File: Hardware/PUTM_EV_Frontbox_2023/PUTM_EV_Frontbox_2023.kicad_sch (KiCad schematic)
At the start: 18 parts, among them J1 Conn_02x16_Counter_Clockwise, J2 Conn_01x04, SW1 Reset switch, U1 STM32G473RCTx

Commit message: Started PCB layout
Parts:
- removed R102: 10k, Resistor_SMD:R_0603_1608Metric_Pad0.98x0.95mm_HandSolder, symbol Device:R_Small
- added H1, H2, H3, H4: MountingHole_Pad, MountingHole:MountingHole_3.2mm_M3_DIN965_Pad_TopBottom, symbol Mechanical:MountingHole_Pad
- J1: footprint (none) -> Connector_PinHeader_2.54mm:PinHeader_2x16_P2.54mm_Vertical
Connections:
- net +24V: now also J1.31 (Pin_31); no longer J1.32 (Pin_32)
- net +5V: now also J1.32 (Pin_32); no longer J1.31 (Pin_31)
- net APPS_POT_1: now also J1.2 (Pin_2); no longer J1.21 (Pin_21)
- net APPS_POT_2: now also J1.1 (Pin_1); no longer J1.20 (Pin_20)
- net BRAKE_POSITION_IN: now also J1.4 (Pin_4); no longer J1.24 (Pin_24)
- net BRAKE_PRESSURE1_IN: now also J1.9 (Pin_9); no longer J1.13 (Pin_13)
- net BSPD_SENSE: now also J1.19 (Pin_19); no longer J1.1 (Pin_1)
- net CAN1+: now also J1.29 (Pin_29); no longer J1.28 (Pin_28)
- net CAN1-: now also J1.28 (Pin_28); no longer J1.29 (Pin_29)
- net CAN2+: now also J1.27 (Pin_27); no longer J1.26 (Pin_26)
- net CAN2-: now also J1.26 (Pin_26); no longer J1.27 (Pin_27)
- net EBS_SAFETY: now also J1.25 (Pin_25); no longer J1.7 (Pin_7)
- net GND: now also R57.1, R58.1, H1.1, H2.1, H3.1, H4.1; no longer R57.2, R58.2
- net INERTIA: now also J1.24 (Pin_24); no longer J1.6 (Pin_6)
- net KILL_KIERA: now also J1.23 (Pin_23); no longer J1.5 (Pin_5)
- net KILL_LEWY: now also J1.22 (Pin_22); no longer J1.4 (Pin_4)
- net KILL_PRAWY: now also J1.20 (Pin_20); no longer J1.2 (Pin_2)
- net OVERTRAVEL: now also J1.21 (Pin_21); no longer J1.3 (Pin_3)
- net SAFE-IN: now also J1.13 (Pin_13); no longer J1.8 (Pin_8)
- net SAFE-OUT: now also J1.14 (Pin_14); no longer J1.9 (Pin_9)
- net STEERING_POSITION_IN: now also J1.5 (Pin_5); no longer J1.25 (Pin_25)
- net SUSPENSION_POT1_IN: now also J1.11 (Pin_11); no longer J1.19 (Pin_19)
- net SUSPENSION_POT2_IN: now also J1.10 (Pin_10); no longer J1.14 (Pin_14)
- net at R48.2: now also J1.18 (Pin_18); no longer J1.11 (Pin_11)
- net at R6.2: now also J1.17 (Pin_17); no longer J1.10 (Pin_10)
- net at J1.15 (Pin_15): now also R58.2
- net at J1.16 (Pin_16): now also R57.2
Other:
- removed sheet Brake Position Potentiometer
- removed sheet Steering Wheel Angle
- added sheet Brake Position (suspension_potentiometer.kicad_sch)
- added sheet CAN bus1 (can_bus.kicad_sch)
- added sheet Steering Position (suspension_potentiometer.kicad_sch)
- sheet APPS1 ports: added 3V3_POT1; removed none
- sheet APPS2: file APPS1.kicad_sch -> APPS2.kicad_sch
- sheet APPS2 ports: added 3V3_POT2, OUT1; removed OUT2
- note added: "APPS Measurement"
- note added: "Analog Inputs"
- note added: "CAN Bus"
- note added: "Debug LEDs"
- note added: "Digital Inputs"
- note added: "MCU"
- note added: "MCU Circutry"
- note added: "Main Connector"
- note added: "Mounting Holes"
- note added: "Power Supply"
- note added: "SC Control"
- note added: "SC sensing"
- note removed: "Horizontal goldpin connector"
- company: Author: Szymon Kostrubiec -> Author: Adam Wasilewski
- moved on the sheet: C1, D1, D2, D3, D4, J2, R1, R2, R3, R4, R48, R57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

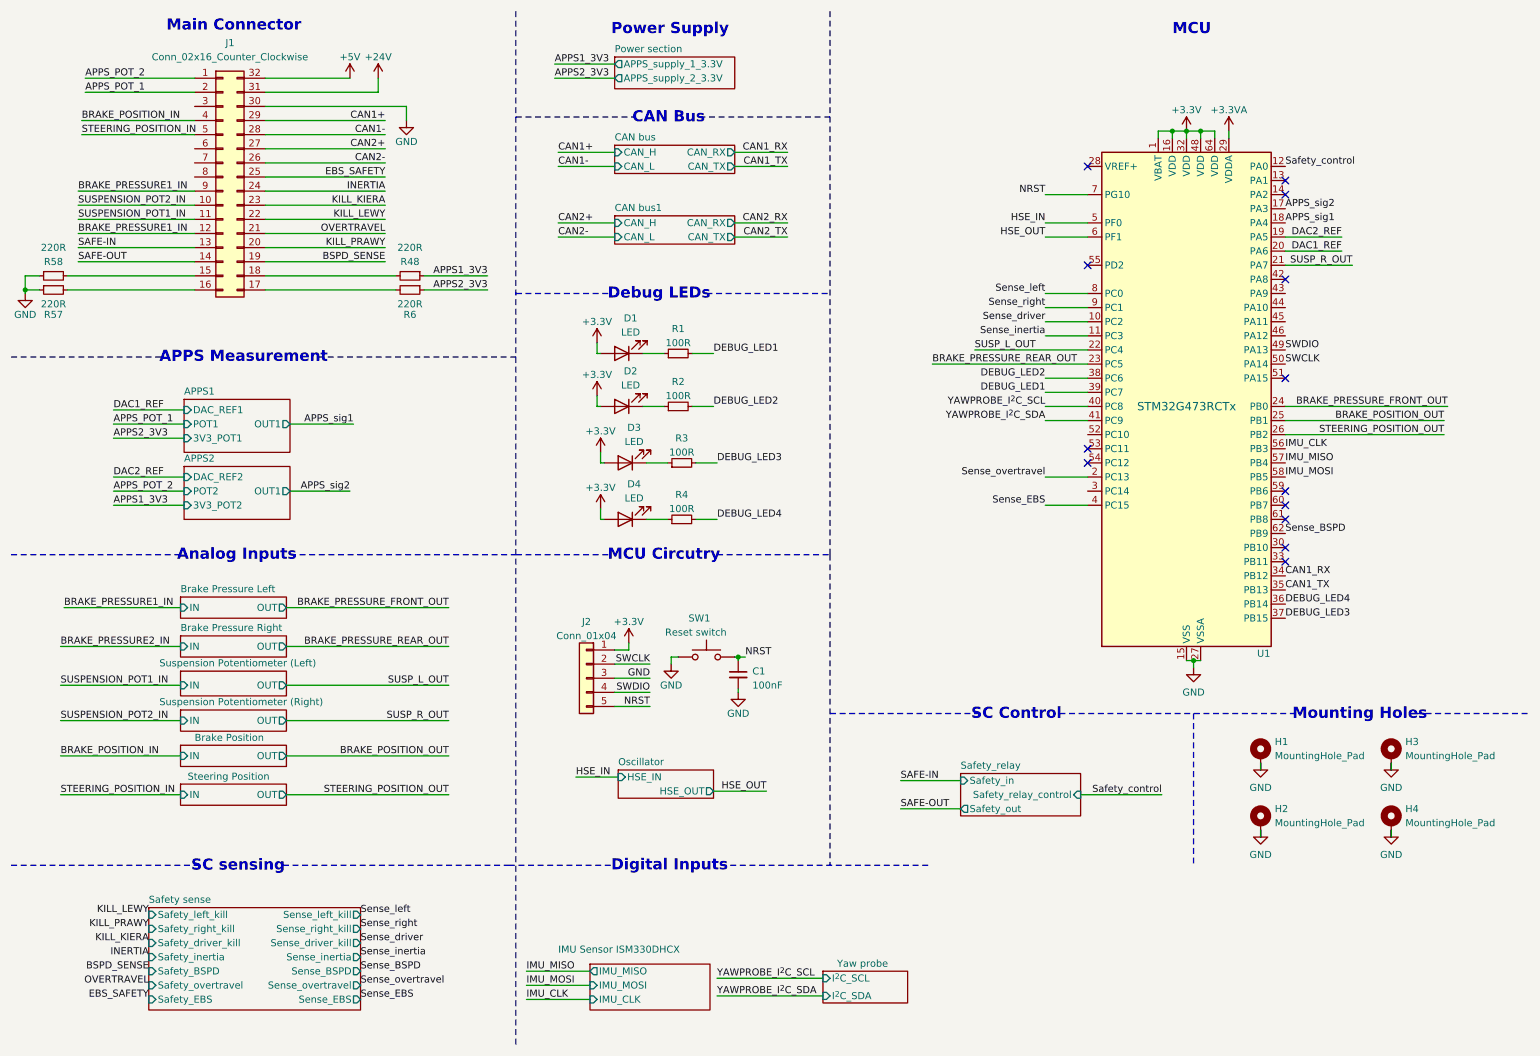
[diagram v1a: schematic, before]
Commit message: Changed board outline and layout to match ASB
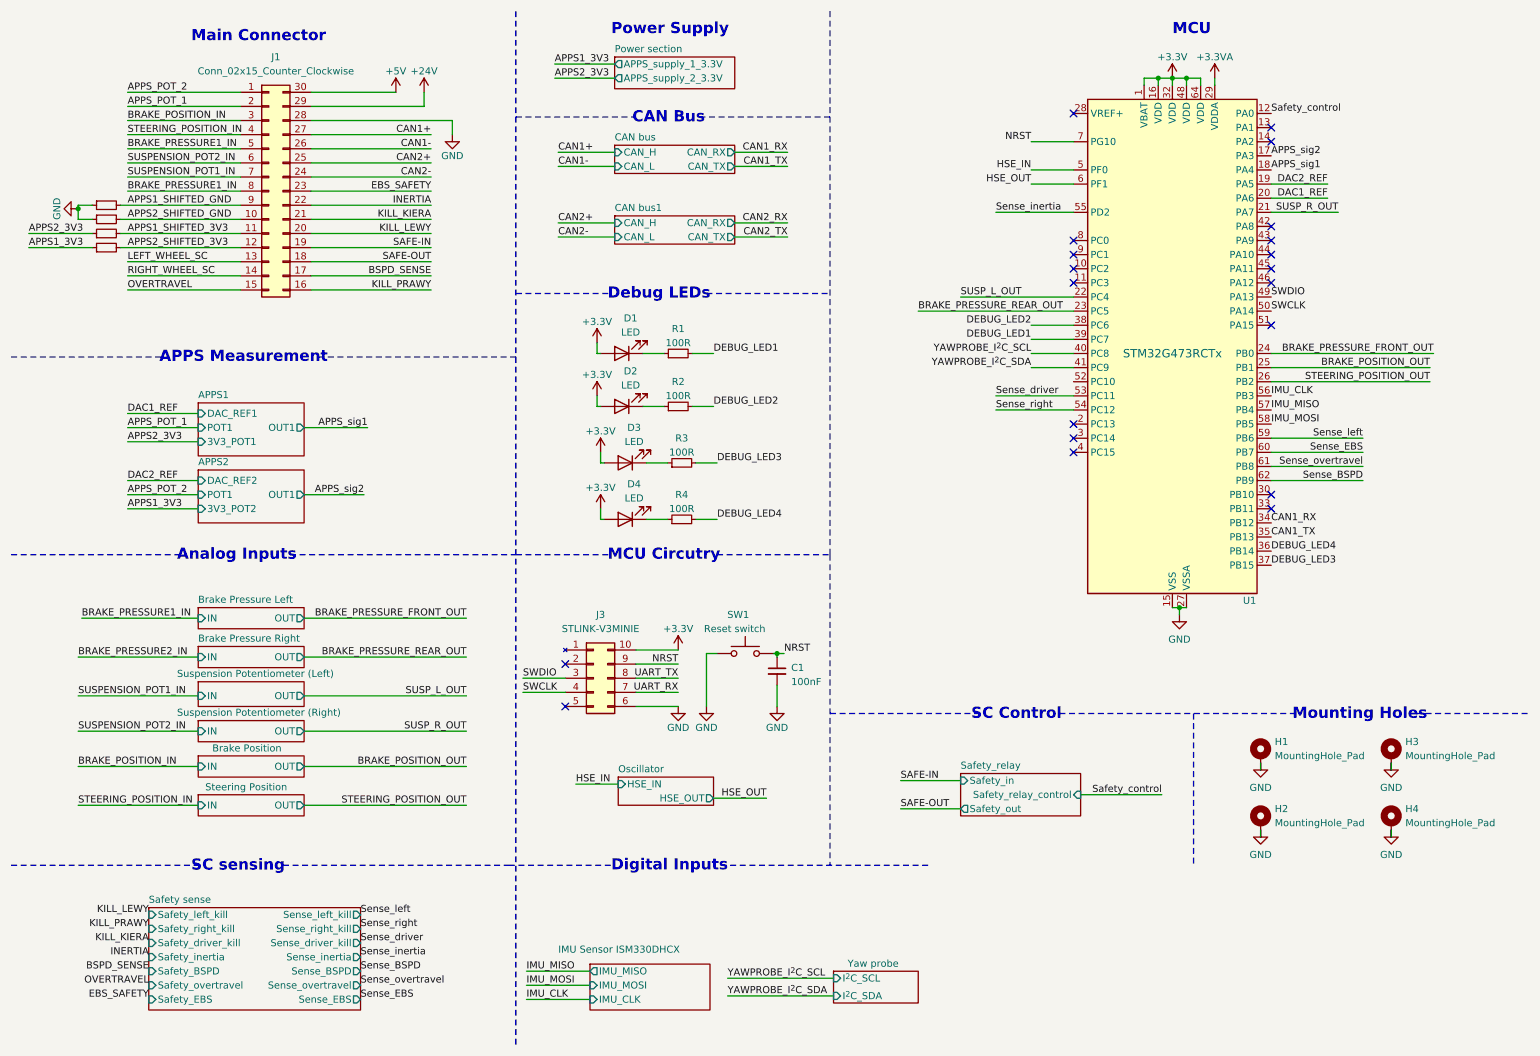
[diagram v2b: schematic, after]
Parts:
- removed J1: Conn_02x16_Counter_Clockwise, Connector_PinHeader_2.54mm:PinHeader_2x16_P2.54mm_Vertical, symbol Connector_Generic:Conn_02x16_Counter_Clockwise
- removed J2: Conn_01x04, Connector_PinHeader_2.54mm:PinHeader_1x05_P2.54mm_Vertical, symbol Connector_Generic:Conn_01x05
- added J1: Conn_02x15_Counter_Clockwise, Connector_IDC:IDC-Header_2x15-1MP_P2.54mm_Latch6.5mm_Vertical, symbol Connector_Generic:Conn_02x15_Counter_Clockwise
- added J3: STLINK-V3MINIE, Frontbox:STLINK-V3MINIE, symbol FrontBox:STLINK-V3MINIE
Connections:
- net +24V: now also J1.29 (Pin_29)
- net +3.3V: now also J3.10 (T_VCC)
- net +5V: now also J1.30 (Pin_30)
- net APPS_POT_1: now also J1.2 (Pin_2)
- net APPS_POT_2: now also J1.1 (Pin_1)
- net BRAKE_POSITION_IN: now also J1.3 (Pin_3)
- net BRAKE_PRESSURE1_IN: now also J1.5 (Pin_5), J1.8 (Pin_8)
- net BSPD_SENSE: now also J1.17 (Pin_17)
- net CAN1+: now also J1.27 (Pin_27)
- net CAN1-: now also J1.26 (Pin_26)
- net CAN2+: now also J1.25 (Pin_25)
- net CAN2-: now also J1.24 (Pin_24)
- net EBS_SAFETY: now also J1.23 (Pin_23)
- net GND: now also J1.28 (Pin_28), J3.6 (GND)
- net INERTIA: now also J1.22 (Pin_22)
- net KILL_KIERA: now also J1.21 (Pin_21)
- net KILL_LEWY: now also J1.20 (Pin_20)
- net KILL_PRAWY: now also J1.16 (Pin_16)
- net NRST: now also J3.9 (T_NRST)
- net OVERTRAVEL: now also J1.15 (Pin_15)
- net SAFE-IN: now also J1.19 (Pin_19)
- net SAFE-OUT: now also J1.18 (Pin_18)
- net STEERING_POSITION_IN: now also J1.4 (Pin_4)
- net SUSPENSION_POT1_IN: now also J1.7 (Pin_7)
- net SUSPENSION_POT2_IN: now also J1.6 (Pin_6)
- net SWCLK: now also J3.4 (T_JCLK/T_SWCLK)
- net SWDIO: now also J3.3 (T_JTMS/T_SWDIO)
- net Sense_EBS: now also U1.60 (PB7); no longer U1.4 (PC15)
- net Sense_driver: now also U1.53 (PC11); no longer U1.10 (PC2)
- net Sense_inertia: now also U1.55 (PD2); no longer U1.11 (PC3)
- net Sense_left: now also U1.59 (PB6); no longer U1.8 (PC0)
- net Sense_overtravel: now also U1.61 (PB8); no longer U1.2 (PC13)
- net Sense_right: now also U1.54 (PC12); no longer U1.9 (PC1)
- net APPS2_SHIFTED_3V3: now reaches R48.2
- net APPS2_SHIFTED_3V3: now also J1.12 (Pin_12)
- net APPS1_SHIFTED_GND: now reaches R58.2
- net APPS1_SHIFTED_GND: now also J1.9 (Pin_9)
- net APPS2_SHIFTED_GND: now reaches R57.2
- net APPS2_SHIFTED_GND: now also J1.10 (Pin_10)
- net APPS1_SHIFTED_3V3: now reaches R6.2
- net APPS1_SHIFTED_3V3: now also J1.11 (Pin_11)
- new net LEFT_WHEEL_SC: J1.13 (Pin_13)
- new net RIGHT_WHEEL_SC: J1.14 (Pin_14)
- new net UART_RX: J3.7 (T_VCP_RX)
- new net UART_TX: J3.8 (T_VCP_TX)
- no-connect marks 13 -> 20
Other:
- sheet APPS2 ports: added POT1; removed POT2
- moved on the sheet: C1, SW1, U1

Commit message: Routing
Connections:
- net CAN1+: now also J1.25 (Pin_25); no longer J1.27 (Pin_27)
- net CAN1-: now also J1.24 (Pin_24); no longer J1.26 (Pin_26)
- net CAN2+: now also J1.27 (Pin_27); no longer J1.25 (Pin_25)
- net CAN2-: now also J1.26 (Pin_26); no longer J1.24 (Pin_24)
- net EBS_SAFETY: now also J1.19 (Pin_19); no longer J1.23 (Pin_23)
- net INERTIA: now also J1.18 (Pin_18); no longer J1.22 (Pin_22)
- net SAFE-IN: now also J1.23 (Pin_23); no longer J1.19 (Pin_19)
- net SAFE-OUT: now also J1.22 (Pin_22); no longer J1.18 (Pin_18)
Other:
- sheet APPS1 ports: added 3V3_POT, DAC_REF, OUT, POT; removed 3V3_POT1, DAC_REF1, OUT1, POT1
- sheet APPS2: file APPS2.kicad_sch -> APPS1.kicad_sch
- sheet APPS2 ports: added 3V3_POT, DAC_REF, OUT, POT; removed 3V3_POT2, DAC_REF2, OUT1, POT1

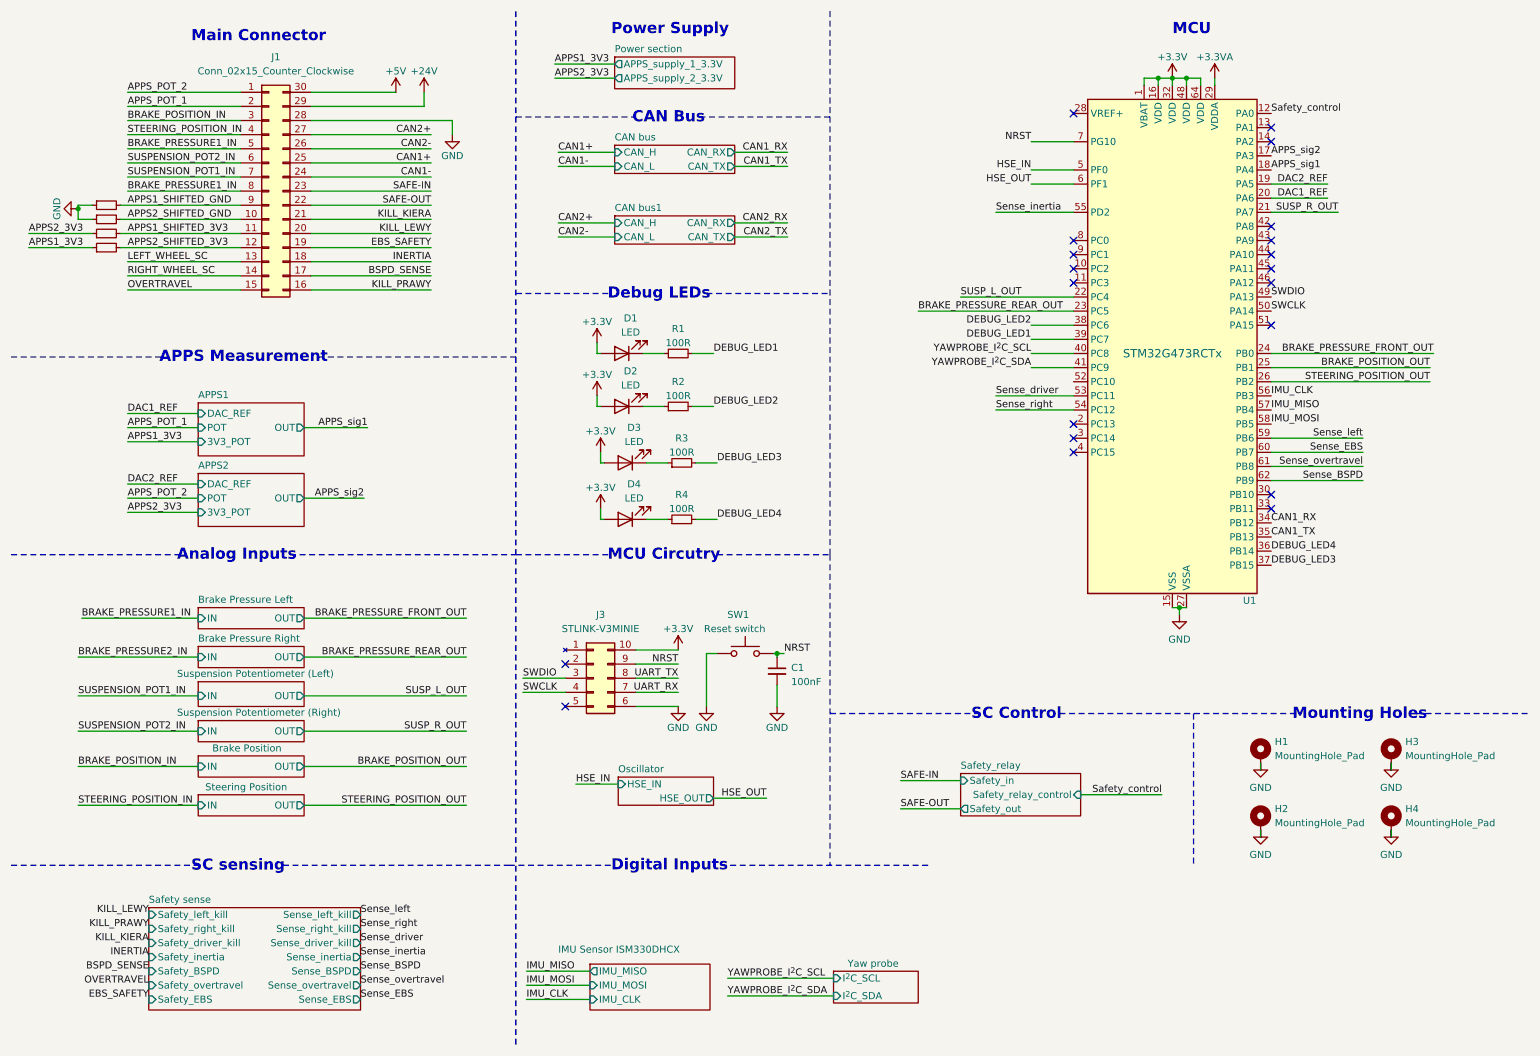
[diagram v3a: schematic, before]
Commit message: Changed mcu pinout
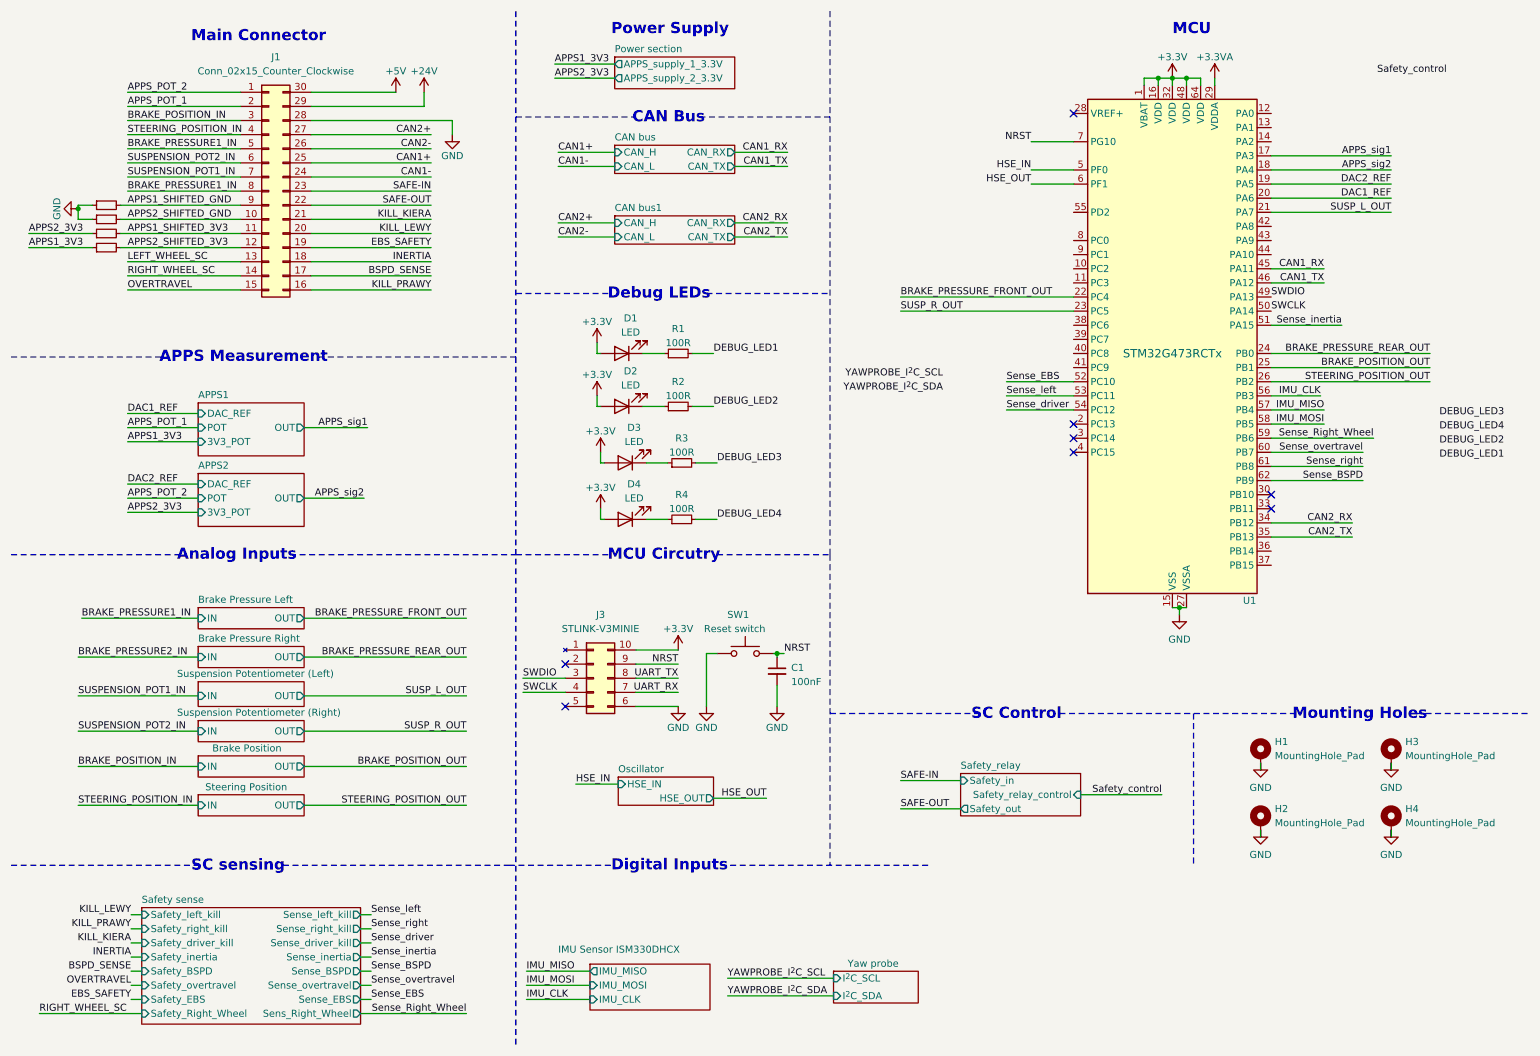
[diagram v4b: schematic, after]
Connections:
- net APPS_sig1: now also U1.17 (PA3); no longer U1.18 (PA4)
- net APPS_sig2: now also U1.18 (PA4); no longer U1.17 (PA3)
- net BRAKE_PRESSURE_FRONT_OUT: now also U1.22 (PC4); no longer U1.24 (PB0)
- net BRAKE_PRESSURE_REAR_OUT: now also U1.24 (PB0); no longer U1.23 (PC5)
- net CAN1_RX: now also U1.45 (PA11); no longer U1.34 (PB12)
- net CAN1_TX: now also U1.46 (PA12); no longer U1.35 (PB13)
- net CAN2_RX: now also U1.34 (PB12)
- net CAN2_TX: now also U1.35 (PB13)
- net DEBUG_LED1: no longer U1.39 (PC7)
- net DEBUG_LED2: no longer U1.38 (PC6)
- net DEBUG_LED3: no longer U1.37 (PB15)
- net DEBUG_LED4: no longer U1.36 (PB14)
- net SUSP_L_OUT: now also U1.21 (PA7); no longer U1.22 (PC4)
- net SUSP_R_OUT: now also U1.23 (PC5); no longer U1.21 (PA7)
- net Safety_control: no longer U1.12 (PA0)
- net Sense_EBS: now also U1.52 (PC10); no longer U1.60 (PB7)
- net Sense_driver: now also U1.54 (PC12); no longer U1.53 (PC11)
- net Sense_inertia: now also U1.51 (PA15); no longer U1.55 (PD2)
- net Sense_left: now also U1.53 (PC11); no longer U1.59 (PB6)
- net Sense_overtravel: now also U1.60 (PB7); no longer U1.61 (PB8)
- net Sense_right: now also U1.61 (PB8); no longer U1.54 (PC12)
- net YAWPROBE_I^{2}C_SCL: no longer U1.40 (PC8)
- net YAWPROBE_I^{2}C_SDA: no longer U1.41 (PC9)
- new net Sense_Right_Wheel: U1.59 (PB6)
- no-connect marks 20 -> 8
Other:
- sheet Safety sense ports: added Safety_Right_Wheel, Sens_Right_Wheel; removed none

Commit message: routing done
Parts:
- removed C1: 100nF, Capacitor_SMD:C_0402_1005Metric_Pad0.74x0.62mm_HandSolder, symbol Device:C_Small
- removed SW1: Reset switch, Button_Switch_SMD:SW_MEC_5GSH9, symbol Switch:SW_MEC_5G
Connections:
- net APPS_sig1: now also U1.18 (PA4); no longer U1.17 (PA3)
- net APPS_sig2: now also U1.17 (PA3); no longer U1.18 (PA4)
- net BRAKE_POSITION_IN: now also J1.7 (Pin_7); no longer J1.3 (Pin_3)
- net BRAKE_POSITION_OUT: now also U1.26 (PB2); no longer U1.25 (PB1)
- net BRAKE_PRESSURE1_IN: now also J1.3 (Pin_3); no longer J1.5 (Pin_5), J1.8 (Pin_8)
- net BRAKE_PRESSURE2_IN: now also J1.8 (Pin_8)
- net BRAKE_PRESSURE_REAR_OUT: now also U1.21 (PA7); no longer U1.24 (PB0)
- net DEBUG_LED1: now also U1.39 (PC7)
- net DEBUG_LED2: now also U1.38 (PC6)
- net DEBUG_LED3: now also U1.37 (PB15)
- net DEBUG_LED4: now also U1.36 (PB14)
- net STEERING_POSITION_IN: now also J1.5 (Pin_5); no longer J1.4 (Pin_4)
- net STEERING_POSITION_OUT: now also U1.24 (PB0); no longer U1.26 (PB2)
- net SUSPENSION_POT1_IN: now also J1.4 (Pin_4); no longer J1.7 (Pin_7)
- net SUSP_L_OUT: now also U1.23 (PC5); no longer U1.21 (PA7)
- net SUSP_R_OUT: now also U1.25 (PB1); no longer U1.23 (PC5)
- net UART_RX: now also U1.44 (PA10)
- net UART_TX: now also U1.43 (PA9)
- net IMU_SCL: now reaches U1.40 (PC8)
- net IMU_SDA: now reaches U1.41 (PC9)
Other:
- removed sheet Yaw probe
- sheet IMU Sensor ISM330DHCX ports: added IMU_SCL, IMU_SDA; removed IMU_CLK, IMU_MISO, IMU_MOSI
- moved on the sheet: J3
